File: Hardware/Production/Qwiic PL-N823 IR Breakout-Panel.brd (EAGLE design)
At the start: 97.3 x 97.3 mm, 354 parts, among them U1 ADS1015, U10 ADS1015, U11 LMV358, U12 PL-N823-01, U13 ADS1015, U14 LMV358, U15 PL-N823-01, U16 ADS1015, U17 LMV358, U18 PL-N823-01, U19 ADS1015, U2 LMV358, U20 LMV358, U21 PL-N823-01, U22 ADS1015, U23 LMV358, U24 PL-N823-01, U25 ADS1015, U26 LMV358, U27 PL-N823-01, U3 PL-N823-01, U4 ADS1015, U5 LMV358, U6 PL-N823-01, U7 ADS1015, U8 LMV358, U9 PL-N823-01

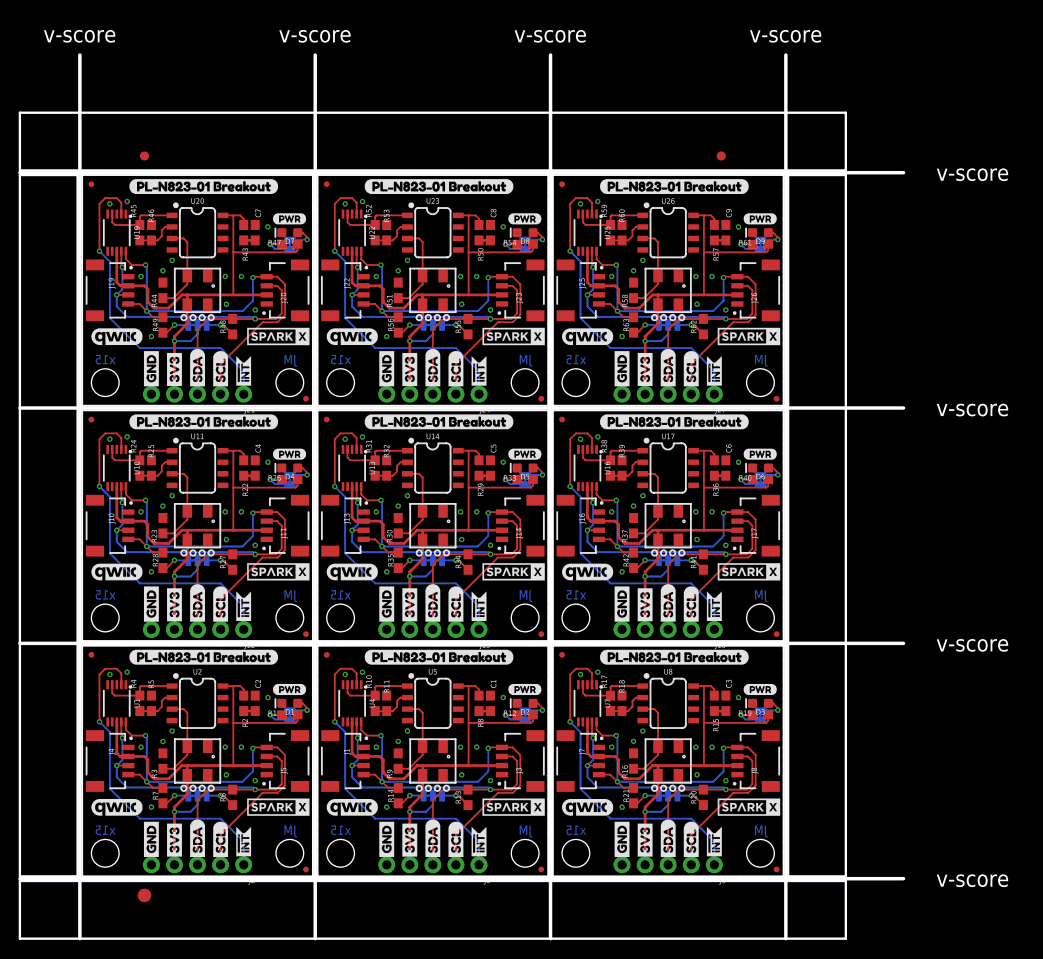
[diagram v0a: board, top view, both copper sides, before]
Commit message: New panel and output files with correct amp circuit
Changed amplification gain factor
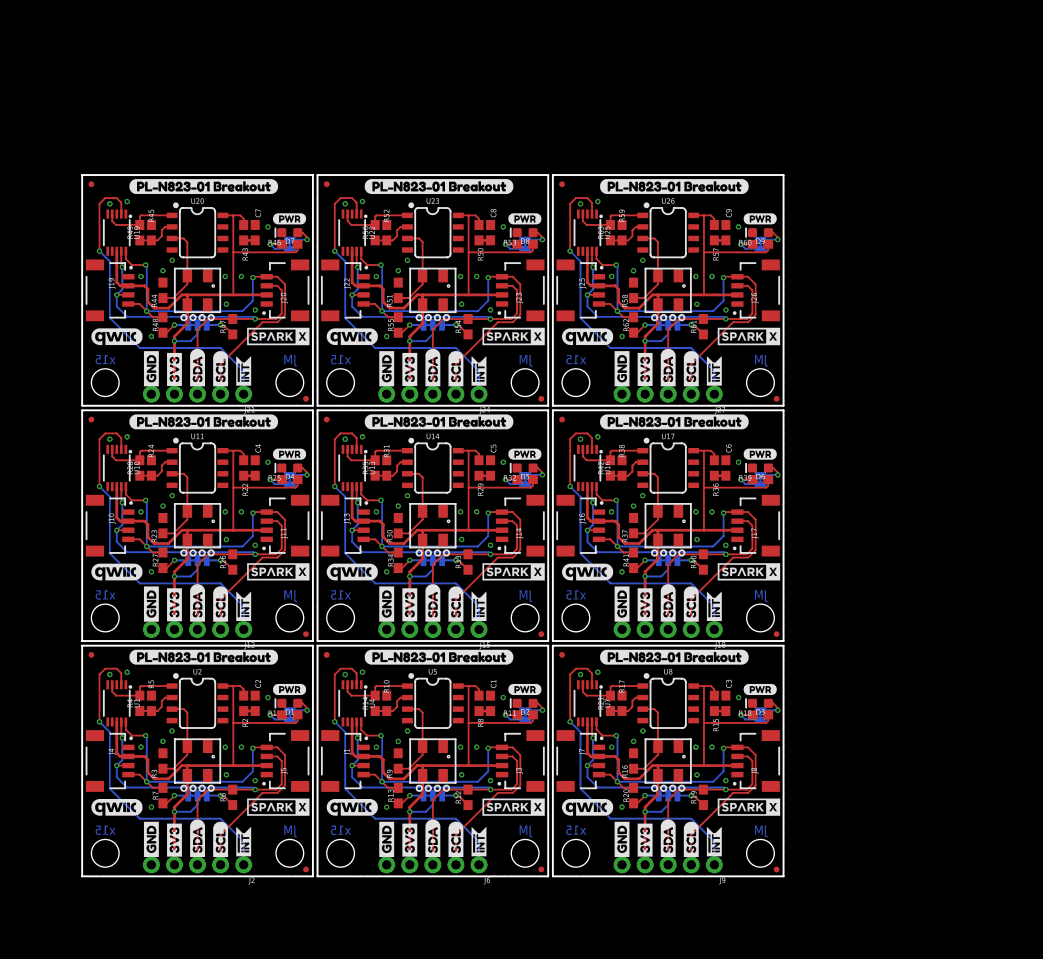
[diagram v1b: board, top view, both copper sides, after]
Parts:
- removed E$1, E$2: (no value), SparkFun-Aesthetics:FIDUCIAL-1X2
- removed E$3: (no value), SparkFun-Retired:FIDUCIAL-1.5X3
- added U$154, U$155: (no value), Labels:3V3-04
- added U$156, U$157: (no value), Labels:GND-04
- added U$158: (no value), buzzard_labels_pln82301:PL#N823#01_BREAKOUT0
- added U$159: (no value), Labels:I_SUPER2_C-()-03
- added U$160, U$161: (no value), Labels:INT#-[<-04
- added U$162: (no value), SparkFun-Aesthetics:PRODUCTION_INSTRUCTIONS
- D1, D2, D3, D4, D5, D6, D7, D8, D9: value RED -> BLUE
- R10, R17, R24, R31, R38, R45, R52, R59: value 4.7k -> 1k
- R11, R18, R25, R32, R39, R46, R53, R60: value 1k -> 27
- R12, R19, R26, R33, R40, R47, R54, R61: value 27 -> 2.2k
- R14, R21, R28, R35, R42, R49, R56, R63: value 2.2k -> 1.20k
- R4: value 4.7k -> 1.20k
- U$100, U$83: device Labels:I_SUPER2_C-()-03 -> Labels:3V3-04
- U$101, U$118, U$119, U$136: device Labels:INT#-[<-04 -> Labels:3V3-04
- U$102, U$67, U$84, U$85: device Labels:INT#-[<-04 -> Labels:GND-04
- U$103, U$120: device SparkFun-Aesthetics:OSHW-LOGO-S -> Labels:GND-04
- U$105: device SparkX:SPARKX-SMALL -> Labels:I_SUPER2_C-()-03
- U$106, U$89: device Labels:QWIIC_COPYRIGHT_SMALL -> Labels:INT#-[<-04
- U$107, U$124: device Labels:PWR-()-03 -> Labels:INT#-[<-04
- U$108, U$144: device Labels:SDA-[) -> SparkFun-Aesthetics:PRODUCTION_INSTRUCTIONS
- U$109, U$145: device Labels:SCL-[) -> SparkFun-Aesthetics:OSHW-LOGO-S
- U$110, U$74: device Labels:SDA-[) -> buzzard_labels_pln82301:PL#N823#01_BREAKOUT0
- U$111, U$75: device Labels:SCL-[) -> SparkX:SPARKX-SMALL
- U$112, U$130: device Labels:3V3-04 -> Labels:QWIIC_COPYRIGHT_SMALL
- U$113, U$95: device Labels:3V3-04 -> Labels:PWR-()-03
- U$114, U$132, U$80, U$98: device Labels:GND-04 -> Labels:SDA-[)
- U$115, U$63, U$81, U$97: device Labels:GND-04 -> Labels:SCL-[)
- U$116, U$150: device buzzard_labels_pln82301:PL#N823#01_BREAKOUT0 -> Labels:SDA-[)
- U$117, U$151: device Labels:I_SUPER2_C-()-03 -> Labels:SCL-[)
- U$121, U$138, U$31, U$48: device buzzard_labels_pln82301:PL#N823#01_BREAKOUT0 -> Labels:GND-04
- U$122, U$20: device SparkX:SPARKX-SMALL -> buzzard_labels_pln82301:PL#N823#01_BREAKOUT0
- U$123: device Labels:QWIIC_COPYRIGHT_SMALL -> Labels:I_SUPER2_C-()-03
- U$125, U$142: device Labels:SDA-[) -> Labels:INT#-[<-04
- U$126: device Labels:SCL-[) -> SparkFun-Aesthetics:PRODUCTION_INSTRUCTIONS
- U$127, U$91: device Labels:SDA-[) -> SparkFun-Aesthetics:OSHW-LOGO-S
- U$128, U$92: device Labels:SCL-[) -> buzzard_labels_pln82301:PL#N823#01_BREAKOUT0
- U$129, U$147: device Labels:3V3-04 -> SparkX:SPARKX-SMALL
- U$131, U$149: device Labels:GND-04 -> Labels:PWR-()-03
- U$133, U$99: device buzzard_labels_pln82301:PL#N823#01_BREAKOUT0 -> Labels:SCL-[)
- U$134: device Labels:I_SUPER2_C-()-03 -> Labels:SDA-[)
- U$135, U$153: device Labels:INT#-[<-04 -> Labels:SCL-[)
- U$137: device SparkFun-Aesthetics:OSHW-LOGO-S -> Labels:3V3-04
- U$139: device SparkX:SPARKX-SMALL -> Labels:GND-04
- U$140, U$38: device Labels:QWIIC_COPYRIGHT_SMALL -> buzzard_labels_pln82301:PL#N823#01_BREAKOUT0
- U$141: device Labels:PWR-()-03 -> Labels:I_SUPER2_C-()-03
- U$143: device Labels:SCL-[) -> Labels:INT#-[<-04
- U$146: device Labels:3V3-04 -> buzzard_labels_pln82301:PL#N823#01_BREAKOUT0
- U$148: device Labels:GND-04 -> Labels:QWIIC_COPYRIGHT_SMALL
- U$152: device Labels:INT#-[<-04 -> Labels:SDA-[)
- U$19: device buzzard_labels_pln82301:PL#N823#01_BREAKOUT0 -> SparkFun-Aesthetics:OSHW-LOGO-S
- U$21: device Labels:QWIIC_COPYRIGHT_SMALL -> SparkX:SPARKX-SMALL
- U$22: device Labels:PWR-()-03 -> Labels:QWIIC_COPYRIGHT_SMALL
- U$23, U$59: device Labels:SDA-[) -> Labels:PWR-()-03
- U$24, U$26, U$60: device Labels:SCL-[) -> Labels:SDA-[)
- U$25: device Labels:SDA-[) -> Labels:SCL-[)
- U$27, U$45, U$61, U$79: device Labels:3V3-04 -> Labels:SCL-[)
- U$29, U$46, U$47, U$64: device Labels:GND-04 -> Labels:3V3-04
- U$3: device SparkFun-Aesthetics:OSHW-LOGO-S -> SparkFun-Aesthetics:PRODUCTION_INSTRUCTIONS
- U$32: device Labels:I_SUPER2_C-()-03 -> buzzard_labels_pln82301:PL#N823#01_BREAKOUT0
- U$33, U$51: device Labels:INT#-[<-04 -> Labels:I_SUPER2_C-()-03
- U$35, U$52: device SparkFun-Aesthetics:OSHW-LOGO-S -> Labels:INT#-[<-04
- U$36: device buzzard_labels_pln82301:PL#N823#01_BREAKOUT0 -> SparkFun-Aesthetics:PRODUCTION_INSTRUCTIONS
- U$37: device SparkX:SPARKX-SMALL -> SparkFun-Aesthetics:OSHW-LOGO-S
- U$39: device Labels:PWR-()-03 -> SparkX:SPARKX-SMALL
- U$40, U$76: device Labels:SDA-[) -> Labels:QWIIC_COPYRIGHT_SMALL
- U$41, U$77: device Labels:SCL-[) -> Labels:PWR-()-03
- U$44, U$62, U$78, U$96: device Labels:3V3-04 -> Labels:SDA-[)
- U$49, U$66: device Labels:I_SUPER2_C-()-03 -> Labels:GND-04
- U$50, U$68: device Labels:INT#-[<-04 -> buzzard_labels_pln82301:PL#N823#01_BREAKOUT0
- U$53, U$70: device buzzard_labels_pln82301:PL#N823#01_BREAKOUT0 -> Labels:INT#-[<-04
- U$54: device SparkX:SPARKX-SMALL -> SparkFun-Aesthetics:PRODUCTION_INSTRUCTIONS
- U$55: device Labels:QWIIC_COPYRIGHT_SMALL -> SparkFun-Aesthetics:OSHW-LOGO-S
- U$56: device Labels:PWR-()-03 -> buzzard_labels_pln82301:PL#N823#01_BREAKOUT0
- U$57, U$93: device Labels:SDA-[) -> SparkX:SPARKX-SMALL
- U$58, U$94: device Labels:SCL-[) -> Labels:QWIIC_COPYRIGHT_SMALL
- U$65, U$82: device buzzard_labels_pln82301:PL#N823#01_BREAKOUT0 -> Labels:3V3-04
- U$69: device SparkFun-Aesthetics:OSHW-LOGO-S -> Labels:I_SUPER2_C-()-03
- U$71, U$88: device SparkX:SPARKX-SMALL -> Labels:INT#-[<-04
- U$72: device Labels:QWIIC_COPYRIGHT_SMALL -> SparkFun-Aesthetics:PRODUCTION_INSTRUCTIONS
- U$73: device Labels:PWR-()-03 -> SparkFun-Aesthetics:OSHW-LOGO-S
- U$86: device SparkFun-Aesthetics:OSHW-LOGO-S -> buzzard_labels_pln82301:PL#N823#01_BREAKOUT0
- U$87: device buzzard_labels_pln82301:PL#N823#01_BREAKOUT0 -> Labels:I_SUPER2_C-()-03
- U$90: device Labels:PWR-()-03 -> SparkFun-Aesthetics:PRODUCTION_INSTRUCTIONS
- moved U$53 80.7 mm to (69.6, 1.52), flipped to the bottom, turned to 90 degrees
- moved U$52 74.3 mm to (69.6, 1.52), flipped to the top, turned to 90 degrees
- moved U$104 74.0 mm to (73.4, 47.5), flipped to the bottom
- moved U$106 73.2 mm to (69.6, 27.4), turned to 90 degrees
- moved U$108 71.0 mm to (79.8, 76.7), turned to 0 degrees
- moved U$107 66.2 mm to (69.6, 27.4), flipped to the bottom, turned to 90 degrees
- moved U$103 65.2 mm to (59.4, 27.6), turned to 90 degrees
- moved U$54 60.7 mm to (79.8, 50.8)
- moved U$126 50.9 mm to (27.9, 102.6), turned to 0 degrees
- moved U$144 50.3 mm to (53.8, 102.6), flipped to the top, turned to 0 degrees
- moved U$105 49.9 mm to (65.9, 36.6), flipped to the bottom
- moved U$72 43.2 mm to (27.9, 76.7)
- moved U$3 43.2 mm to (27.9, 50.8), flipped to the top
- moved U$139 40.3 mm to (33.5, 53.5), flipped to the bottom, turned to 90 degrees
- moved U$90 35.7 mm to (53.8, 76.7)
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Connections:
- net 3.3V1: now also R11.2; no longer R12.2
- net 3.3V2: now also R18.2; no longer R19.2
- net 3.3V3: now also R25.2; no longer R26.2
- net 3.3V4: now also R32.2; no longer R33.2
- net 3.3V5: now also R39.2; no longer R40.2
- net 3.3V6: now also R46.2; no longer R47.2
- net 3.3V7: now also R53.2; no longer R54.2
- net 3.3V8: now also R60.2; no longer R61.2
- net GND1: now also R10.1; no longer R11.1
- net GND2: now also R17.1; no longer R18.1
- net GND3: now also R24.1; no longer R25.1
- net GND4: now also R31.1; no longer R32.1
- net GND5: now also R38.1; no longer R39.1
- net GND6: now also R45.1; no longer R46.1
- net GND7: now also R52.1; no longer R53.1
- net GND8: now also R59.1; no longer R60.1
- net N$10: now also R12.1; no longer R13.1
- net N$12: now also R11.1; no longer R12.1
- net N$14: now also R17.2, R21.1; no longer R17.1, R18.2
- net N$15: now also R20.1; no longer R21.1
- net N$16: now also R19.1; no longer R20.1
- net N$18: now also R18.1; no longer R19.1
- net N$20: now also R24.2, R28.1; no longer R24.1, R25.2
- net N$21: now also R27.1; no longer R28.1
- net N$22: now also R26.1; no longer R27.1
- net N$24: now also R25.1; no longer R26.1
- net N$26: now also R31.2, R35.1; no longer R31.1, R32.2
- net N$27: now also R34.1; no longer R35.1
- net N$28: now also R33.1; no longer R34.1
- net N$30: now also R32.1; no longer R33.1
- net N$32: now also R38.2, R42.1; no longer R38.1, R39.2
- net N$33: now also R41.1; no longer R42.1
- net N$34: now also R40.1; no longer R41.1
- net N$36: now also R39.1; no longer R40.1
- net N$38: now also R45.2, R49.1; no longer R45.1, R46.2
- net N$39: now also R48.1; no longer R49.1
- net N$40: now also R47.1; no longer R48.1
- net N$42: now also R46.1; no longer R47.1
- net N$44: now also R52.2, R56.1; no longer R52.1, R53.2
- net N$45: now also R55.1; no longer R56.1
- net N$46: now also R54.1; no longer R55.1
- net N$48: now also R53.1; no longer R54.1
- net N$50: now also R59.2, R63.1; no longer R59.1, R60.2
- net N$51: now also R62.1; no longer R63.1
- net N$52: now also R61.1; no longer R62.1
- net N$54: now also R60.1; no longer R61.1
- net N$8: now also R10.2, R14.1; no longer R10.1, R11.2
- net N$9: now also R13.1; no longer R14.1
- net SCL1: now also R13.2; no longer R14.2
- net SCL2: now also R20.2; no longer R21.2
- net SCL3: now also R27.2; no longer R28.2
- net SCL4: now also R34.2; no longer R35.2
- net SCL5: now also R41.2; no longer R42.2
- net SCL6: now also R48.2; no longer R49.2
- net SCL7: now also R55.2; no longer R56.2
- net SCL8: now also R62.2; no longer R63.2
- net SDA1: now also R12.2; no longer R13.2
- net SDA2: now also R19.2; no longer R20.2
- net SDA3: now also R26.2; no longer R27.2
- net SDA4: now also R33.2; no longer R34.2
- net SDA5: now also R40.2; no longer R41.2
- net SDA6: now also R47.2; no longer R48.2
- net SDA7: now also R54.2; no longer R55.2
- net SDA8: now also R61.2; no longer R62.2
- net SIGNAL1: now also R14.2; no longer R10.2
- net SIGNAL2: now also R21.2; no longer R17.2
- net SIGNAL3: now also R28.2; no longer R24.2
- net SIGNAL4: now also R35.2; no longer R31.2
- net SIGNAL5: now also R42.2; no longer R38.2
- net SIGNAL6: now also R49.2; no longer R45.2
- net SIGNAL7: now also R56.2; no longer R52.2
- net SIGNAL8: now also R63.2; no longer R59.2
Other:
- board size 97.3 x 97.3 mm -> 77.2 x 77.2 mm
- board text added: "Max reflow temp is 240C"
- board text added: "No clean"
- board text removed: "v-score"
